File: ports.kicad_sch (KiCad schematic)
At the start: 8 parts, among them J1 Power, J2 Lamp, J3 BDU DISPLAY, J4 Sound, J5 Switch Matrix, J6 Cabinet, J7 Solenoid, J9 DISPLAY

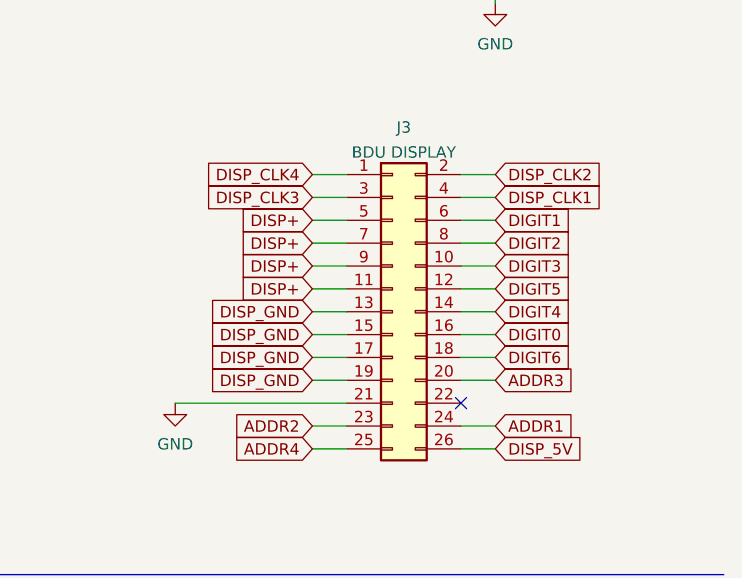
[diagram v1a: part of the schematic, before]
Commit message: Update BDU connector
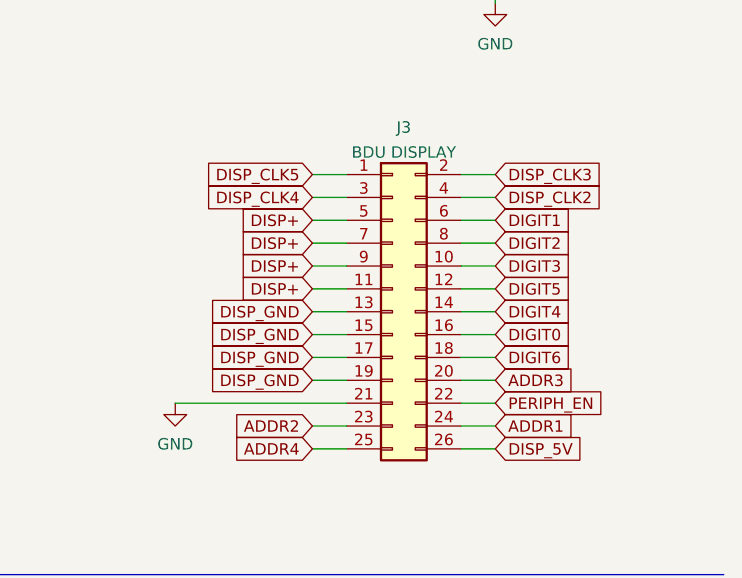
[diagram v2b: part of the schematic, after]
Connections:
- net DISP_CLK1: no longer J3.4 (Pin_4)
- net DISP_CLK2: now also J3.4 (Pin_4); no longer J3.2 (Pin_2)
- net DISP_CLK3: now also J3.2 (Pin_2); no longer J3.3 (Pin_3)
- net DISP_CLK4: now also J3.3 (Pin_3); no longer J3.1 (Pin_1)
- net DISP_CLK5: now also J3.1 (Pin_1)
- net PERIPH_EN: now also J3.22 (Pin_22)
- no-connect marks 11 -> 10
